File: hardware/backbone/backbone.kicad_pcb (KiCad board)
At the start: 4 copper layers, 31.3 x 68.9 mm, 75 parts, among them J1 M20-7810645R, J140 M20-7810645R, J2 FROM_PREVIOUS, J3 M20-7810645R, J4 SM04B-SRSS-TB(LF)(SN), J5 FH12-24S-0.5SH(55), J9 TO NEXT, Q2 AO3401A, U1 ESP32-S3-WROOM-1_1U_FlexyPin_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, U2 SN65HVD230DR, U3 HC-TYPE-C-16P-01A, U4 TPS562201DDCR, U8 G3VM-61VY3

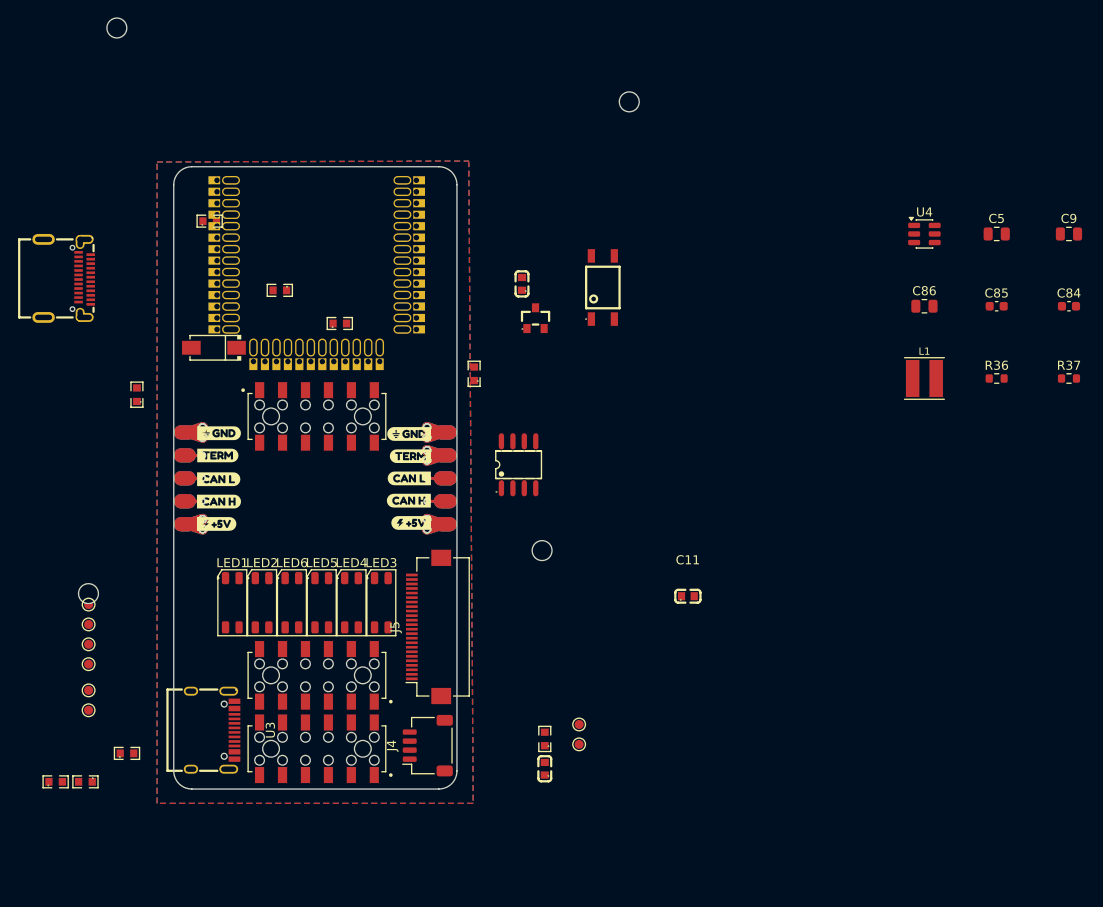
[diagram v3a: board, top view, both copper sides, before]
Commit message: hardware: add configurable ports and LCSC component libraries
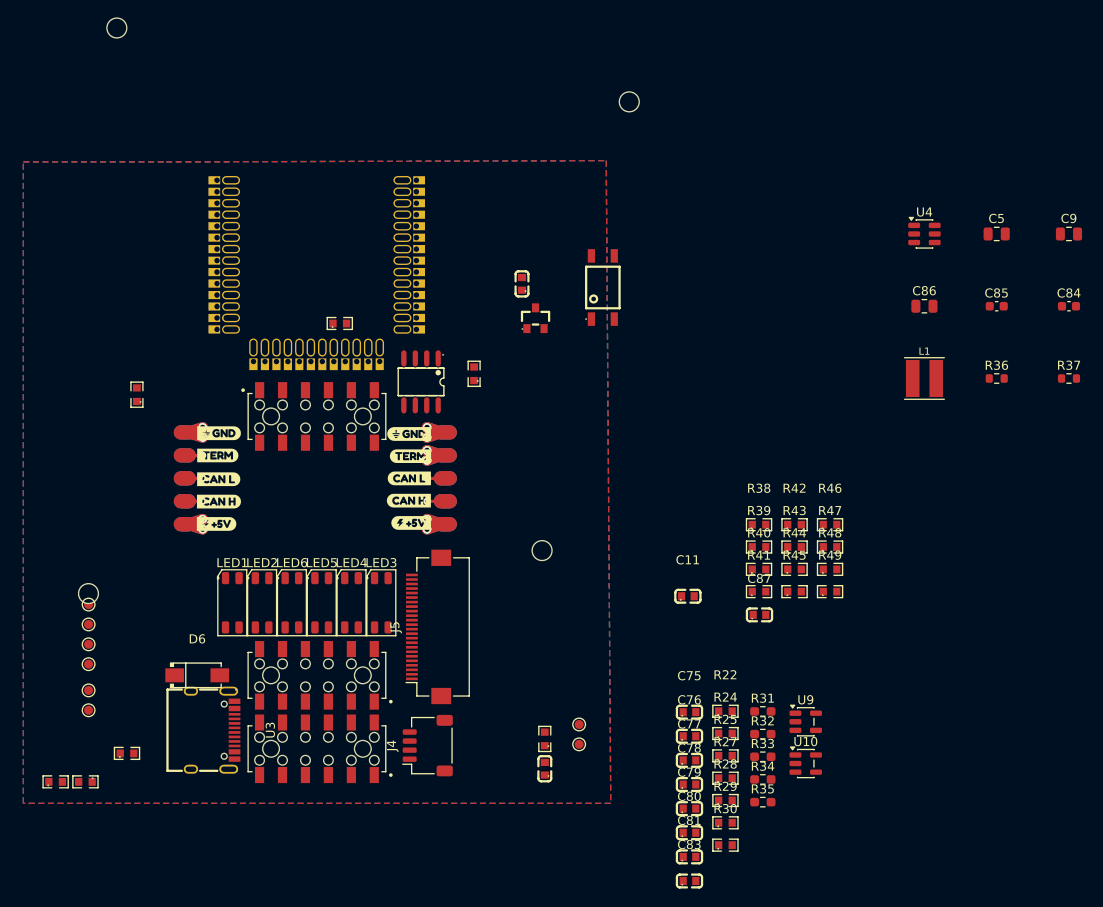
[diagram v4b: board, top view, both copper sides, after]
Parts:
- removed D4: SS54_C22452, SpaghettiLAB:SMA_L4.4-W2.8-LS5.4-R-RD
- removed R20, R23: 5.1k, SpaghettiLAB:R0603
- removed USB1: TYPEC-324G-BCP24, SpaghettiLAB:USB-C-SMD_TYPEC-324G-BCP24
- added C75: 4.7uF/10V X7R, SpaghettiLAB:C0603, F.Cu at (209.0, 122.9)
- added C76: 4.7uF/10V X7R, SpaghettiLAB:C0603, F.Cu at (209.0, 125.6)
- added C77: 4.7uF/10V X7R, SpaghettiLAB:C0603, F.Cu at (209.0, 128.3)
- added C78: 4.7uF/10V X7R, SpaghettiLAB:C0603, F.Cu at (209.0, 130.9)
- added C79: 100nF, SpaghettiLAB:C0603, F.Cu at (209.0, 133.6)
- added C80: 100nF, SpaghettiLAB:C0603, F.Cu at (209.0, 136.3)
- added C81: 100nF, SpaghettiLAB:C0603, F.Cu at (209.0, 139.0)
- added C83: 100nF, SpaghettiLAB:C0603, F.Cu at (209.0, 141.6)
- added C87: 100nF, SpaghettiLAB:C0603, F.Cu at (216.7, 112.2)
- added D6: SS54_C22452, SpaghettiLAB:SMA_L4.4-W2.8-LS5.4-R-RD, F.Cu at (154.5, 118.9)
- added R22: 5.1k, SpaghettiLAB:R0603, F.Cu at (213.0, 122.8)
- added R24: 4.7k, SpaghettiLAB:R0603, F.Cu at (213.0, 125.3)
- added R25: 4.7k, SpaghettiLAB:R0603, F.Cu at (213.0, 127.8)
- added R27: 5.1k, SpaghettiLAB:R0603, F.Cu at (213.0, 130.2)
- added R28: 10k, SpaghettiLAB:R0603, F.Cu at (213.0, 132.7)
- added R29: 10k, SpaghettiLAB:R0603, F.Cu at (213.0, 135.2)
- added R30: 0, SpaghettiLAB:R0603, F.Cu at (213.0, 137.7)
- added R31: 0R, Resistor_SMD:R_0603_1608Metric_Pad0.98x0.95mm_HandSolder, F.Cu at (217.1, 122.9)
- added R32: 0R, Resistor_SMD:R_0603_1608Metric_Pad0.98x0.95mm_HandSolder, F.Cu at (217.1, 125.4)
- added R33: 0R, Resistor_SMD:R_0603_1608Metric_Pad0.98x0.95mm_HandSolder, F.Cu at (217.1, 127.9)
- added R34: 0R, Resistor_SMD:R_0603_1608Metric_Pad0.98x0.95mm_HandSolder, F.Cu at (217.1, 130.4)
- added R35: 0R, Resistor_SMD:R_0603_1608Metric_Pad0.98x0.95mm_HandSolder, F.Cu at (217.1, 132.9)
- added R38: 100k, SpaghettiLAB:R0603, F.Cu at (216.7, 102.2)
- added R39: 100k, SpaghettiLAB:R0603, F.Cu at (216.7, 104.7)
- added R40: 100k, SpaghettiLAB:R0603, F.Cu at (216.7, 107.1)
- added R41: 100k, SpaghettiLAB:R0603, F.Cu at (216.7, 109.6)
- added R42: 100k, SpaghettiLAB:R0603, F.Cu at (220.6, 102.2)
- added R43: 100k, SpaghettiLAB:R0603, F.Cu at (220.6, 104.7)
- added R44: 100k, SpaghettiLAB:R0603, F.Cu at (220.6, 107.1)
- added R45: 100k, SpaghettiLAB:R0603, F.Cu at (220.6, 109.6)
- added R46: 100k, SpaghettiLAB:R0603, F.Cu at (224.6, 102.2)
- added R47: 100k, SpaghettiLAB:R0603, F.Cu at (224.6, 104.7)
- added R48: 100k, SpaghettiLAB:R0603, F.Cu at (224.6, 107.1)
- added R49: 100k, SpaghettiLAB:R0603, F.Cu at (224.6, 109.6)
- added U10: ME6211C15M5G-N, Package_TO_SOT_SMD:SOT-23-5, F.Cu at (221.9, 128.6)
- added U9: ME6211C28M5G-N, Package_TO_SOT_SMD:SOT-23-5, F.Cu at (221.9, 124.0)
- moved U2 14.2 mm to (179.3, 86.4), turned to 180 degrees
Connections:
- C1 pad 2: GND -> Net-(USB1-CC1)
- C11 pad 1: GND -> Net-(USB1-CC1)
- C5 pad 2: GND -> Net-(USB1-CC1)
- C74 pad 1: GND -> Net-(USB1-CC1)
- C85 pad 2: GND -> Net-(USB1-CC1)
- C86 pad 2: GND -> Net-(USB1-CC1)
- C9 pad 2: GND -> Net-(USB1-CC1)
- J1 pad 1: Net-(J1-Pad1) -> A0
- J1 pad 10: Net-(J1-Pad10) -> A4
- J1 pad 11: Net-(J1-Pad11) -> A5
- J1 pad 12: Net-(J1-Pad11) -> A5
- J1 pad 2: Net-(J1-Pad1) -> A0
- J1 pad 3: Net-(J1-Pad3) -> A1
- J1 pad 4: Net-(J1-Pad3) -> A1
- J1 pad 5: Net-(J1-Pad5) -> A2
- J1 pad 6: Net-(J1-Pad5) -> A2
- J1 pad 7: Net-(J1-Pad7) -> A3
- J1 pad 8: Net-(J1-Pad7) -> A3
- J1 pad 9: Net-(J1-Pad10) -> A4
- J140 pad 1: Net-(J1-Pad1) -> A0
- J140 pad 10: Net-(J1-Pad10) -> A4
- J140 pad 11: Net-(J1-Pad11) -> A5
- J140 pad 12: Net-(J1-Pad11) -> A5
- J140 pad 2: Net-(J1-Pad1) -> A0
- J140 pad 3: Net-(J1-Pad3) -> A1
- J140 pad 4: Net-(J1-Pad3) -> A1
- J140 pad 5: Net-(J1-Pad5) -> A2
- J140 pad 6: Net-(J1-Pad5) -> A2
- J140 pad 7: Net-(J1-Pad7) -> A3
- J140 pad 8: Net-(J1-Pad7) -> A3
- J140 pad 9: Net-(J1-Pad10) -> A4
- J2 pad 5: GND -> Net-(USB1-CC1)
- J3 pad 3: GND -> Net-(USB1-CC1)
- J3 pad 4: GND -> Net-(USB1-CC1)
- J4 pad 1: unconnected-(J4-GND-Pad1) -> Net-(USB1-CC1)
- J4 pad 2: unconnected-(J4-+3V3-Pad2) -> VCORE
- J4 pad 3: unconnected-(J4-SDA-Pad3) -> IO4
- J4 pad 4: unconnected-(J4-SCL-Pad4) -> IO5
- J5 pad 1: unconnected-(J5-Pad1) -> FPC_3V3
- J5 pad 10: unconnected-(J5-Pad10) -> +1V5
- J5 pad 11: unconnected-(J5-Pad11) -> +2V8
- J5 pad 12: unconnected-(J5-Pad12) -> IO21
- J5 pad 13: unconnected-(J5-Pad13) -> FPC_CLK
- J5 pad 14: unconnected-(J5-Pad14) -> IO18
- J5 pad 15: unconnected-(J5-Pad15) -> Net-(USB1-CC1)
- J5 pad 16: unconnected-(J5-Pad16) -> IO17
- J5 pad 17: unconnected-(J5-Pad17) -> IO2
- J5 pad 18: unconnected-(J5-Pad18) -> IO42
- J5 pad 19: unconnected-(J5-Pad19) -> IO38
- J5 pad 2: unconnected-(J5-Pad2) -> Net-(USB1-CC1)
- J5 pad 20: unconnected-(J5-Pad20) -> IO41
- J5 pad 21: unconnected-(J5-Pad21) -> IO39
- J5 pad 22: unconnected-(J5-Pad22) -> IO40
- J5 pad 23: unconnected-(J5-Pad23) -> FPC_TX
- J5 pad 24: unconnected-(J5-Pad24) -> FPC_RX
- J5 pad 3: unconnected-(J5-Pad3) -> IO4
- J5 pad 4: unconnected-(J5-Pad4) -> +2V8
- J5 pad 5: unconnected-(J5-Pad5) -> IO5
- J5 pad 6: unconnected-(J5-Pad6) -> FPC_PULLUP
- J5 pad 7: unconnected-(J5-Pad7) -> IO6
- J5 pad 8: unconnected-(J5-Pad8) -> FPC_PULLDOWN
- J5 pad 9: unconnected-(J5-Pad9) -> IO1
- J9 pad 5: GND -> Net-(USB1-CC1)
- LED1 pad 1: GND -> Net-(USB1-CC1)
- LED2 pad 1: GND -> Net-(USB1-CC1)
- LED3 pad 1: GND -> Net-(USB1-CC1)
- LED4 pad 1: GND -> Net-(USB1-CC1)
- LED5 pad 1: GND -> Net-(USB1-CC1)
- LED6 pad 1: GND -> Net-(USB1-CC1)
- R37 pad 2: GND -> Net-(USB1-CC1)
- R4 pad 1: GND -> Net-(USB1-CC1)
- TP12 pad 1: GND -> Net-(USB1-CC1)
- TP13 pad 1: GND -> Net-(USB1-CC1)
- TP21 pad 1: GND -> Net-(USB1-CC1)
- U1 pad 1: GND -> Net-(USB1-CC1)
- U1 pad 40: GND -> Net-(USB1-CC1)
- U2 pad 2: GND -> Net-(USB1-CC1)
- U2 pad 8: GND -> Net-(USB1-CC1)
- U3 pad 1: unconnected-(U3-SHELL-Pad1) -> Net-(USB1-CC1)
- U3 pad 2: unconnected-(U3-SHELL-Pad2) -> Net-(USB1-CC1)
- U3 pad 3: unconnected-(U3-SHELL-Pad3) -> Net-(USB1-CC1)
- U3 pad 4: unconnected-(U3-SHELL-Pad4) -> Net-(USB1-CC1)
- U3 pad A1B12: unconnected-(U3-GND-PadA1B12) -> Net-(USB1-CC1)
- U3 pad A4B9: unconnected-(U3-VBUS-PadA4B9) -> VBUS
- U3 pad A5: unconnected-(U3-CC1-PadA5) -> Net-(U3-CC1)
- U3 pad A6: unconnected-(U3-D+-PadA6) -> USB_D+
- U3 pad A7: unconnected-(U3-D--PadA7) -> USB_D-
- U3 pad B1A12: unconnected-(U3-GND-PadB1A12) -> Net-(USB1-CC1)
- U3 pad B4A9: unconnected-(U3-VBUS-PadB4A9) -> VBUS
- U3 pad B5: unconnected-(U3-CC2-PadB5) -> Net-(U3-CC2)
- U3 pad B6: unconnected-(U3-D+-PadB6) -> USB_D+
- U3 pad B7: unconnected-(U3-D--PadB7) -> USB_D-
- U4 pad 1: GND -> Net-(USB1-CC1)
- U8 pad 2: GND -> Net-(USB1-CC1)
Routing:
- net Net-(USB1-CC1): track 0.00 -> 13.9 mm, vias 0 -> 4
- net GND: track 13.9 -> 0.00 mm, vias 4 -> 0
- added copper zone on B.Cu, net Net-(USB1-CC1)
- added copper zone on F.Cu, net Net-(USB1-CC1)
- added copper zone on In2.Cu, net Net-(USB1-CC1)
- removed copper zone on B.Cu, net GND
- removed copper zone on F.Cu, net GND
- removed copper zone on In2.Cu, net GND
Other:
- board outline removed

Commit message: Use AG32 internal converters and place backbone hardware
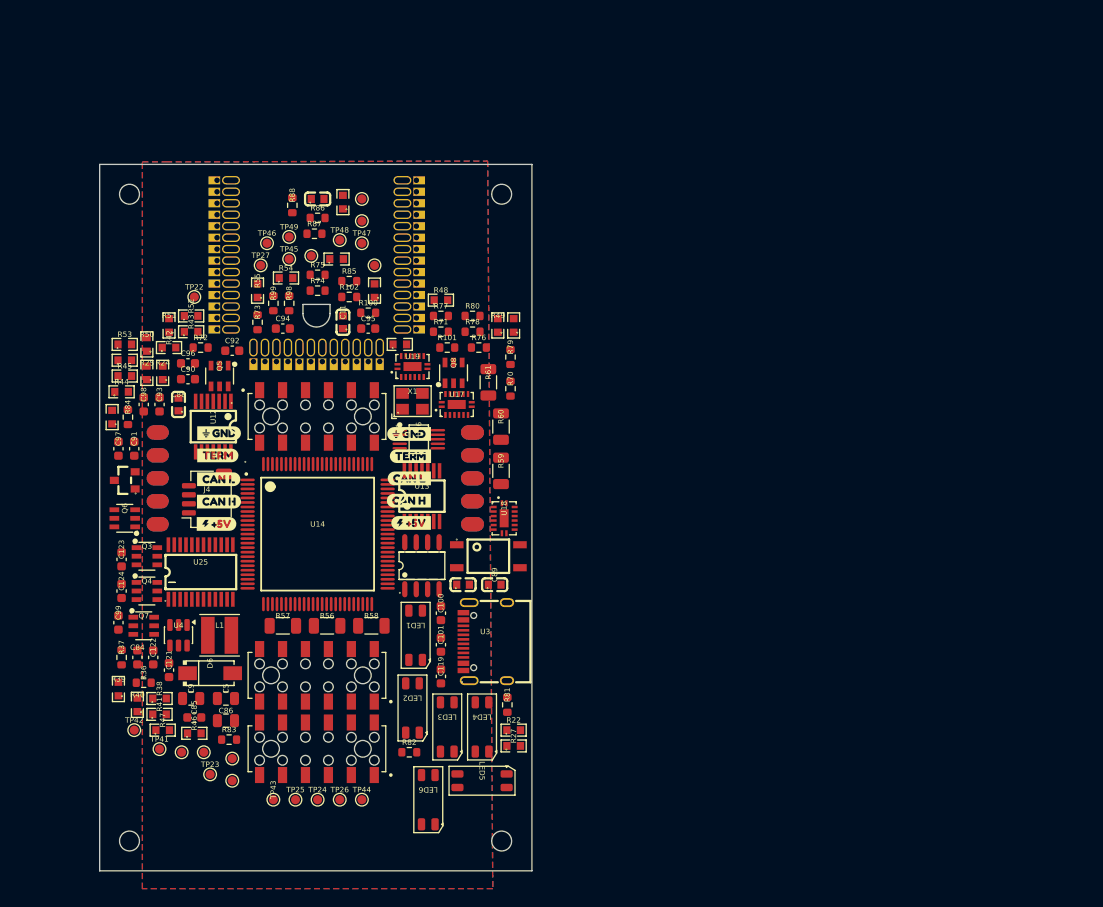
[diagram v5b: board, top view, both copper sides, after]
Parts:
- removed C75, C76, C77, C78: 4.7uF/10V X7R, SpaghettiLAB:C0603
- removed C79, C80, C81, C83, C87: 100nF, SpaghettiLAB:C0603
- removed J5: FH12-24S-0.5SH(55), SpaghettiLAB:Hirose_FH12-24S-0.5SH_1x24-1MP_P0.50mm_Horizontal
- removed R28, R29: 10k, SpaghettiLAB:R0603
- removed R30: 0, SpaghettiLAB:R0603
- removed R31, R32, R33, R34, R35: 0R, Resistor_SMD:R_0603_1608Metric_Pad0.98x0.95mm_HandSolder
- removed U10: ME6211C15M5G-N, Package_TO_SOT_SMD:SOT-23-5
- removed U9: ME6211C28M5G-N, Package_TO_SOT_SMD:SOT-23-5
- added C100: 100nF, Capacitor_SMD:C_0603_1608Metric, F.Cu at (181.5, 112.0)
- added C101: 100nF, Capacitor_SMD:C_0603_1608Metric, F.Cu at (181.5, 115.5)
- added C119: 100nF, Capacitor_SMD:C_0603_1608Metric, F.Cu at (181.5, 119.0)
- added C121: 100nF, Capacitor_SMD:C_0603_1608Metric, F.Cu at (151.4, 118.3)
- added C122: 100nF, Capacitor_SMD:C_0603_1608Metric, F.Cu at (149.6, 116.9)
- added C123: 100nF, Capacitor_SMD:C_0603_1608Metric, F.Cu at (146.1, 106.0)
- added C124: 100nF, Capacitor_SMD:C_0603_1608Metric, F.Cu at (146.1, 109.5)
- added C88: 100nF, SpaghettiLAB:C0603, F.Cu at (152.4, 88.9)
- added C89: 100nF, SpaghettiLAB:C0603, F.Cu at (187.4, 108.8)
- added C90: 100nF, Capacitor_SMD:C_0603_1608Metric, F.Cu at (153.5, 86.1)
- added C91: 100nF, Capacitor_SMD:C_0603_1608Metric, F.Cu at (147.5, 93.8)
- added C92: 100nF, Capacitor_SMD:C_0603_1608Metric, F.Cu at (158.4, 82.9)
- added C93: 100nF, Capacitor_SMD:C_0603_1608Metric, F.Cu at (150.3, 88.9)
- added C94: 100nF, Capacitor_SMD:C_0603_1608Metric, F.Cu at (164.0, 80.5)
- added C95: 100nF, Capacitor_SMD:C_0603_1608Metric, F.Cu at (173.4, 80.5)
- added C96: 100nF, Capacitor_SMD:C_0603_1608Metric, F.Cu at (153.5, 84.3)
- added C97: 100nF, Capacitor_SMD:C_0603_1608Metric, F.Cu at (145.8, 93.8)
- added C98: 100nF, Capacitor_SMD:C_0603_1608Metric, F.Cu at (148.6, 88.9)
- added C99: 1uF, Capacitor_SMD:C_0603_1608Metric, F.Cu at (145.8, 113.0)
- added Q3: AO6604, LCSC_Ports:SOT-23-6_L2.9-W1.6-P0.95-LS2.8-BL, F.Cu at (148.9, 105.7)
- added Q4: AO6604, LCSC_Ports:SOT-23-6_L2.9-W1.6-P0.95-LS2.8-BL, F.Cu at (148.9, 109.5)
- added Q5: AO6604, LCSC_Ports:SOT-23-6_L2.9-W1.6-P0.95-LS2.8-BL, F.Cu at (157.0, 85.7)
- added Q6: AO6604, LCSC_Ports:SOT-23-6_L2.9-W1.6-P0.95-LS2.8-BL, F.Cu at (146.5, 101.5)
- added Q7: AO6604, LCSC_Ports:SOT-23-6_L2.9-W1.6-P0.95-LS2.8-BL, F.Cu at (148.6, 113.4)
- added Q8: AO6604, LCSC_Ports:SOT-23-6_L2.9-W1.6-P0.95-LS2.8-BL, F.Cu at (182.9, 85.4)
- added R100: 0R / ESP-only, Resistor_SMD:R_0603_1608Metric, F.Cu at (173.4, 78.7)
- added R101: 0R / ESP-only, Resistor_SMD:R_0603_1608Metric, F.Cu at (182.2, 82.6)
- added R102: 0R / ESP-only, Resistor_SMD:R_0603_1608Metric, F.Cu at (171.3, 77.0)
- added R50: 100k, SpaghettiLAB:R0603, F.Cu at (148.9, 82.2)
- added R51: 100k, SpaghettiLAB:R0603, F.Cu at (151.4, 80.1)
- added R52: 100k, SpaghettiLAB:R0603, F.Cu at (153.8, 79.1)
- added R53: 100k, SpaghettiLAB:R0603, F.Cu at (146.5, 82.2)
- added R54: 100k, SpaghettiLAB:R0603, F.Cu at (164.3, 74.9)
- added R55: 100k, SpaghettiLAB:R0603, F.Cu at (161.2, 76.3)
- added R56: 0.1R, Resistor_SMD:R_1206_3216Metric, F.Cu at (168.9, 113.4)
- added R57: 0.1R, Resistor_SMD:R_1206_3216Metric, F.Cu at (164.0, 113.4)
- added R58: 0.1R, Resistor_SMD:R_1206_3216Metric, F.Cu at (173.8, 113.4)
- added R59: 0.1R, Resistor_SMD:R_1206_3216Metric, F.Cu at (188.1, 96.2)
- added R60: 0.1R, Resistor_SMD:R_1206_3216Metric, F.Cu at (188.1, 91.3)
- added R61: 0.1R, Resistor_SMD:R_1206_3216Metric, F.Cu at (186.7, 86.4)
- added R70: 100k, Resistor_SMD:R_0603_1608Metric, F.Cu at (189.2, 87.1)
- added R71: 100k, Resistor_SMD:R_0603_1608Metric, F.Cu at (181.5, 80.8)
- added R72: 10k, Resistor_SMD:R_0603_1608Metric, F.Cu at (154.9, 82.6)
- added R73: 10k, Resistor_SMD:R_0603_1608Metric, F.Cu at (161.2, 79.8)
- added R74: 100k, Resistor_SMD:R_0603_1608Metric, F.Cu at (167.8, 76.3)
- added R75: 100k, Resistor_SMD:R_0603_1608Metric, F.Cu at (167.8, 74.5)
- added R76: 100k, Resistor_SMD:R_0603_1608Metric, F.Cu at (185.7, 82.6)
- added R77: 4.7k 0.1% 25ppm, Resistor_SMD:R_0603_1608Metric, F.Cu at (181.5, 79.1)
- added R78: 100k, Resistor_SMD:R_0603_1608Metric, F.Cu at (185.0, 80.8)
- added R79: 4.7k, Resistor_SMD:R_0603_1608Metric, F.Cu at (189.2, 83.6)
- added R80: 4.7k, Resistor_SMD:R_0603_1608Metric, F.Cu at (185.0, 79.1)
- added R81: 22R, Resistor_SMD:R_0603_1608Metric, F.Cu at (188.8, 122.1)
- added R82: 22R, Resistor_SMD:R_0603_1608Metric, F.Cu at (178.0, 127.4)
- added R83: 10k, Resistor_SMD:R_0603_1608Metric, F.Cu at (158.0, 126.0)
- added R84: 10k, Resistor_SMD:R_0603_1608Metric, F.Cu at (146.8, 90.3)
- added R85: 1k, Resistor_SMD:R_0603_1608Metric, F.Cu at (171.3, 75.2)
- added R86: 1k, Resistor_SMD:R_0603_1608Metric, F.Cu at (167.8, 68.2)
- added R87: 1k, Resistor_SMD:R_0603_1608Metric, F.Cu at (167.5, 70.0)
- added R88: 1k, Resistor_SMD:R_0603_1608Metric, F.Cu at (165.0, 66.8)
- added R98: 0R / ESP-only, Resistor_SMD:R_0603_1608Metric, F.Cu at (164.7, 77.7)
- added R99: 0R / ESP-only, Resistor_SMD:R_0603_1608Metric, F.Cu at (162.9, 77.7)
- added TP22: AG_NRST, TestPoint:TestPoint_Pad_D1.0mm, F.Cu at (154.2, 77.0)
- added TP23: AG_JTMS, TestPoint:TestPoint_Pad_D1.0mm, F.Cu at (155.9, 129.8)
- added TP24: AG_JTCK, TestPoint:TestPoint_Pad_D1.0mm, F.Cu at (167.8, 132.6)
- added TP25: AG_JTDI, TestPoint:TestPoint_Pad_D1.0mm, F.Cu at (165.4, 132.6)
- added TP26: AG_JTDO, TestPoint:TestPoint_Pad_D1.0mm, F.Cu at (170.3, 132.6)
- added TP27: AG_JNTRST, TestPoint:TestPoint_Pad_D1.0mm, F.Cu at (161.5, 73.5)
- added TP41: DAC1, TestPoint:TestPoint_Pad_D1.0mm, F.Cu at (150.3, 127.0)
- added TP42: ADC_SPARE_17, TestPoint:TestPoint_Pad_D1.0mm, F.Cu at (147.5, 124.9)
- added TP43: ADC_SPARE_33, TestPoint:TestPoint_Pad_D1.0mm, F.Cu at (162.9, 132.6)
- added TP44: ADC_SPARE_34, TestPoint:TestPoint_Pad_D1.0mm, F.Cu at (172.7, 132.6)
- added TP45: ADC_SPARE_35, TestPoint:TestPoint_Pad_D1.0mm, F.Cu at (164.7, 72.8)
- added TP46: ADC_SPARE_36, TestPoint:TestPoint_Pad_D1.0mm, F.Cu at (162.2, 71.0)
- added TP47: AG_UART_RX, TestPoint:TestPoint_Pad_D1.0mm, F.Cu at (172.7, 71.0)
- added TP48: AG_UART_TX, TestPoint:TestPoint_Pad_D1.0mm, F.Cu at (170.3, 70.7)
- added TP49: AG_BOOT0, TestPoint:TestPoint_Pad_D1.0mm, F.Cu at (164.7, 70.3)
- added U12: SN74CBTLV3125PWR, LCSC_Ports:TSSOP-14_L5.0-W4.4-P0.65-LS6.4-BL, F.Cu at (156.3, 91.3)
- added U13: SN74CBTLV3125PWR, LCSC_Ports:TSSOP-14_L5.0-W4.4-P0.65-LS6.4-BL, F.Cu at (179.4, 99.0)
- added U14: AG32VF407VGT6, LCSC_Ports:LQFP-100_L14.0-W14.0-P0.50-LS16.0-TL, F.Cu at (167.8, 103.2)
- added U16: INA226AIDGSR, LCSC_Ports:MSOP-10_L3.0-W3.0-P0.50-LS5.0-BL, F.Cu at (179.0, 92.7)
- added U17: 74HC4051BQ,115, LCSC_Ports:DHVQFN-16_L3.5-W2.5-P0.50-BL-EP, F.Cu at (183.2, 88.9)
- added U18: 74HC4051BQ,115, LCSC_Ports:DHVQFN-16_L3.5-W2.5-P0.50-BL-EP, F.Cu at (188.5, 101.5)
- added U19: 74HC4051BQ,115, LCSC_Ports:DHVQFN-16_L3.5-W2.5-P0.50-BL-EP, F.Cu at (178.3, 84.7)
- added U25: TCA9535PWR(UMW), LCSC_Ports:TSSOP-24_L7.8-W4.4-P0.65-LS6.4-BL, F.Cu at (154.9, 107.4)
- added X1: 20MHz, LCSC_Ports:OSC-SMD_4P-L3.2-W2.5-BL, F.Cu at (178.3, 88.5)
- R17, R18: value 33R -> 33R DNP / ESP USB
- moved C84 110.2 mm to (147.9, 116.9), turned to 90 degrees
- moved C9 109.9 mm to (153.8, 121.4)
- moved R37 109.3 mm to (146.1, 116.9), turned to 90 degrees
- moved R36 100.3 mm to (148.6, 119.7)
- moved C85 99.8 mm to (154.2, 123.5)
- moved C5 99.6 mm to (157.7, 121.4)
- moved U4 93.8 mm to (152.4, 114.4), turned to -90 degrees
- moved C86 89.9 mm to (157.7, 123.9)
- moved L1 83.0 mm to (157.0, 114.4)
- moved R45 77.9 mm to (146.5, 85.7)
- moved R44 77.0 mm to (146.1, 87.5)
- moved R25 76.8 mm to (148.9, 85.4), turned to 90 degrees
- moved R47 76.6 mm to (150.7, 124.9)
- moved R46 74.1 mm to (154.2, 125.3)
- moved R24 74.0 mm to (150.7, 85.4), turned to 90 degrees
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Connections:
- net /RXD0 renamed SPI_MISO
- net /TXD0 renamed SPI_MOSI
- net /~{RESET} renamed ~{RESET}
- net Net-(LED1-DOUT) renamed /LED_CHAIN_1
- net Net-(LED2-DOUT) renamed /LED_CHAIN_2
- net Net-(LED3-DOUT) renamed /LED_CHAIN_3
- net Net-(LED4-DOUT) renamed /LED_CHAIN_4
- net Net-(LED5-DOUT) renamed /LED_CHAIN_5
- net Net-(U4-SW) renamed /BUCK_SW
- net Net-(U4-VBST) renamed /BUCK_BOOT
- net Net-(U4-VFB) renamed /BUCK_FB
- C1 pad 2: Net-(USB1-CC1) -> GND
- C11 pad 1: Net-(USB1-CC1) -> GND
- C5 pad 2: Net-(USB1-CC1) -> GND
- C74 pad 1: Net-(USB1-CC1) -> GND
- C85 pad 2: Net-(USB1-CC1) -> GND
- C86 pad 2: Net-(USB1-CC1) -> GND
- C9 pad 2: Net-(USB1-CC1) -> GND
- J1 pad 1: A0 -> PORT_A0
- J1 pad 10: A4 -> PORT_A4
- J1 pad 11: A5 -> PORT_A5
- J1 pad 12: A5 -> PORT_A5
- J1 pad 2: A0 -> PORT_A0
- J1 pad 3: A1 -> PORT_A1
- J1 pad 4: A1 -> PORT_A1
- J1 pad 5: A2 -> PORT_A2
- J1 pad 6: A2 -> PORT_A2
- J1 pad 7: A3 -> PORT_A3
- J1 pad 8: A3 -> PORT_A3
- J1 pad 9: A4 -> PORT_A4
- J140 pad 1: A0 -> PORT_A0
- J140 pad 10: A4 -> PORT_A4
- J140 pad 11: A5 -> PORT_A5
- J140 pad 12: A5 -> PORT_A5
- J140 pad 2: A0 -> PORT_A0
- J140 pad 3: A1 -> PORT_A1
- J140 pad 4: A1 -> PORT_A1
- J140 pad 5: A2 -> PORT_A2
- J140 pad 6: A2 -> PORT_A2
- J140 pad 7: A3 -> PORT_A3
- J140 pad 8: A3 -> PORT_A3
- J140 pad 9: A4 -> PORT_A4
- J2 pad 5: Net-(USB1-CC1) -> GND
- J3 pad 10: A2 -> GND
- J3 pad 12: A3 -> A5
- J3 pad 2: 5V -> GND
- J3 pad 3: Net-(USB1-CC1) -> A0
- J3 pad 4: Net-(USB1-CC1) -> A1
- J3 pad 5: A7 -> VCORE
- J3 pad 6: A0 -> GND
- J3 pad 7: A6 -> A2
- J3 pad 8: A1 -> A3
- J3 pad 9: A5 -> VCORE
- J4 pad 1: Net-(USB1-CC1) -> GND
- J9 pad 5: Net-(USB1-CC1) -> GND
- LED1 pad 1: Net-(USB1-CC1) -> GND
- LED2 pad 1: Net-(USB1-CC1) -> GND
- LED3 pad 1: Net-(USB1-CC1) -> GND
- LED4 pad 1: Net-(USB1-CC1) -> GND
- LED5 pad 1: Net-(USB1-CC1) -> GND
- LED6 pad 1: Net-(USB1-CC1) -> GND
- LED6 pad 4: unconnected-(LED6-DOUT-Pad4) -> (no net)
- R22 pad 1: Net-(U3-CC2) -> /USB_CC1
- R22 pad 2: Net-(USB1-CC1) -> GND
- R27 pad 1: Net-(USB1-CC1) -> GND
- R27 pad 2: Net-(U3-CC1) -> /USB_CC2
- R37 pad 2: Net-(USB1-CC1) -> GND
- R38 pad 2: Net-(Q3A-G) -> P_GATE_0
- R39 pad 1: Net-(Q3B-G) -> N_GATE_0
- R39 pad 2: Net-(USB1-CC1) -> GND
- R4 pad 1: Net-(USB1-CC1) -> GND
- R40 pad 2: Net-(Q4A-G) -> P_GATE_1
- R41 pad 1: Net-(Q4B-G) -> N_GATE_1
- R41 pad 2: Net-(USB1-CC1) -> GND
- R42 pad 2: Net-(Q5A-G) -> P_GATE_2
- R43 pad 1: Net-(Q5B-G) -> N_GATE_2
- R43 pad 2: Net-(USB1-CC1) -> GND
- R44 pad 2: Net-(Q6A-G) -> P_GATE_3
- R45 pad 1: Net-(Q6B-G) -> N_GATE_3
- R45 pad 2: Net-(USB1-CC1) -> GND
- R46 pad 2: Net-(Q7A-G) -> P_GATE_4
- R47 pad 1: Net-(Q7B-G) -> N_GATE_4
- R47 pad 2: Net-(USB1-CC1) -> GND
- R48 pad 2: Net-(Q8A-G) -> P_GATE_5
- R49 pad 1: Net-(Q8B-G) -> N_GATE_5
- R49 pad 2: Net-(USB1-CC1) -> GND
- TP12 pad 1: Net-(USB1-CC1) -> GND
- TP13 pad 1: Net-(USB1-CC1) -> GND
- TP21 pad 1: Net-(USB1-CC1) -> GND
- U1 pad 1: Net-(USB1-CC1) -> GND
- U1 pad 19: A4 -> IO11
- U1 pad 20: A5 -> IO12
- U1 pad 21: A6 -> CTRL13
- U1 pad 22: A7 -> CTRL14
- U1 pad 24: CAN_RX -> /ESP_PROG_TX
- U1 pad 25: CAN_TX -> /ESP_PROG_RX
- U1 pad 38: IO2 -> A5
- U1 pad 39: IO1 -> A4
- U1 pad 40: Net-(USB1-CC1) -> GND
- U1 pad 8: IO15 -> /ESP_AG_BOOT0
- U1 pad 9: ALED -> /ESP_AG_RESET_N
- U2 pad 2: Net-(USB1-CC1) -> GND
- U2 pad 5: unconnected-(U2-VREF-Pad5) -> (no net)
- U2 pad 8: Net-(USB1-CC1) -> GND
- U3 pad 1: Net-(USB1-CC1) -> GND
- U3 pad 2: Net-(USB1-CC1) -> GND
- U3 pad 3: Net-(USB1-CC1) -> GND
- U3 pad 4: Net-(USB1-CC1) -> GND
- U3 pad A1B12: Net-(USB1-CC1) -> GND
- U3 pad A5: Net-(U3-CC1) -> /USB_CC1
- U3 pad A8: unconnected-(U3-SBU1-PadA8) -> (no net)
- U3 pad B1A12: Net-(USB1-CC1) -> GND
- U3 pad B5: Net-(U3-CC2) -> /USB_CC2
- U3 pad B8: unconnected-(U3-SBU2-PadB8) -> (no net)
- U4 pad 1: Net-(USB1-CC1) -> GND
- U8 pad 2: Net-(USB1-CC1) -> GND
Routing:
- net 5V: track 20.9 -> 0.00 mm, vias 6 -> 0
- net Net-(USB1-CC1): track 13.9 -> 0.00 mm, vias 4 -> 0
- net CAN_L: track 6.60 -> 0.00 mm, vias 2 -> 0
- net CAN_H: track 6.60 -> 0.00 mm, vias 2 -> 0
- net TERM_CTRL_OUT: track 3.30 -> 0.00 mm, vias 1 -> 0
- added copper zone on B.Cu, net GND
- added copper zone on F.Cu, net GND
- added copper zone on In2.Cu, net GND
- removed copper zone on B.Cu, net Net-(USB1-CC1)
- removed copper zone on F.Cu, net Net-(USB1-CC1)
- removed copper zone on In2.Cu, net Net-(USB1-CC1)
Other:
- board outline added: 47.9 x 78.2 mm
